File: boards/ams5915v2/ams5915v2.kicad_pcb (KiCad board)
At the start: 2 copper layers, 20 x 56.5 mm, 32 parts, among them J1 Conn_01x04, M3 MountingHole_3.2mm_M3, U1 TLV73333PDBVR, U2 MAX4995A, U3 AMS5915, U4 MAX4995A, U5 AMS5915

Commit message: [ams5915v2] new board design
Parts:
- removed 3v3: 3v3, Measurement_Points:Measurement_Point_Round-SMD-Pad_Small
- removed 5v: 5v, Measurement_Points:Measurement_Point_Round-SMD-Pad_Small
- removed GND: GND, Measurement_Points:Measurement_Point_Round-SMD-Pad_Small
- removed M3 (x3): MountingHole_3.2mm_M3, Mounting_Holes:MountingHole_3.2mm_M3
- added REF**: MountingHole_3.2mm_M3, Mounting_Holes:MountingHole_3.2mm_M3, F.Cu at (60.5, 77.5)
- added REF**: MountingHole_3.2mm_M3, Mounting_Holes:MountingHole_3.2mm_M3, F.Cu at (83.0, 68.0)
- added REF**: MountingHole_3.2mm_M3, Mounting_Holes:MountingHole_3.2mm_M3, F.Cu at (105.5, 77.5)
- added TP1: 5v, Measurement_Points:Measurement_Point_Round-SMD-Pad_Small, F.Cu at (105.4, 65.0)
- added TP2: GND, Measurement_Points:Measurement_Point_Round-SMD-Pad_Small, F.Cu at (103.7, 72.9)
- added TP3: 3v3, Measurement_Points:Measurement_Point_Round-SMD-Pad_Small, B.Cu at (96.5, 66.5)
- C1, C2, C3, C4, C5, C6, C7, C8, R1, R2, R5, R6, R7, R8, U1, U2, U4: moved to B.Cu
- moved R7 119.7 mm to (65.9, 75.9), turned to 90 degrees
- moved C8 118.0 mm to (69.2, 76.7)
- moved D4 117.3 mm to (62.2, 70.0), turned to 270 degrees
- moved U5 115.6 mm to (64.2, 80.0), turned to 0 degrees
- moved U4 115.0 mm to (68.8, 73.7), turned to 90 degrees
- moved C5 111.8 mm to (71.5, 72.5), turned to 270 degrees
- moved C6 108.3 mm to (69.2, 78.4), turned to 180 degrees
- moved R8 107.0 mm to (73.0, 71.7)
- moved R5 103.9 mm to (88.4, 75.8), turned to 90 degrees
- moved C7 103.0 mm to (91.6, 76.7)
- moved D3 101.7 mm to (84.3, 73.8), turned to 180 degrees
- moved U2 101.2 mm to (91.1, 73.8), turned to 90 degrees
- moved C3 99.2 mm to (92.8, 71.0)
- moved J1 98.6 mm to (107.1, 65.0), turned to 0 degrees
- moved R6 97.9 mm to (92.1, 69.7), turned to 0 degrees
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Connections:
- net /5v renamed +5V
- net /GND renamed GND
- U1 pad 4: Net-(U1-Pad4) -> (no net)
- U3 pad 5: Net-(U3-Pad5) -> (no net)
- U3 pad 6: Net-(U3-Pad6) -> (no net)
- U3 pad 7: Net-(U3-Pad7) -> (no net)
- U3 pad 8: Net-(U3-Pad8) -> (no net)
- U5 pad 5: Net-(U5-Pad5) -> (no net)
- U5 pad 6: Net-(U5-Pad6) -> (no net)
- U5 pad 7: Net-(U5-Pad7) -> (no net)
- U5 pad 8: Net-(U5-Pad8) -> (no net)
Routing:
- net +5V: track 94.2 -> 14.1 mm, vias 4 -> 0
- net GND: track 126.4 -> 197.9 mm, vias 39 -> 22
- net Net-(C6-Pad1): track 23.1 -> 5.72 mm
- net Net-(C4-Pad1): track 22.7 -> 5.68 mm
- net /3v3: track 64.9 -> 53.5 mm
- net Net-(D1-Pad1): track 12.0 -> 1.55 mm
- net Net-(D4-Pad1): track 1.40 -> 11.5 mm, vias 0 -> 1
- net Net-(D2-Pad2): track 10.5 -> 1.72 mm
- net Net-(D3-Pad1): track 1.25 -> 7.98 mm, vias 0 -> 1
- net Net-(R1-Pad2): track 39.0 -> 34.7 mm, vias 2 -> 1
- net Net-(R2-Pad2): track 39.3 -> 36.8 mm, vias 2 -> 0
- net Net-(R7-Pad2): track 3.54 -> 2.09 mm
- net Net-(R5-Pad2): track 3.28 -> 1.86 mm
- net Net-(R8-Pad2): track 3.87 -> 3.33 mm
- net Net-(R6-Pad2): track 3.82 -> 3.28 mm
- removed copper zone on B.Cu, net +5V
- removed copper zone on B.Cu, net /3v3
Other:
- board size 20 x 56.5 mm -> 52 x 17 mm
- net class Default: trace_width 0.6 -> 0.25
- board text added: "+3V3"
- board text added: "+5V"
- board text added: "GND"
- board text added: "Over current"
- board text added: "SCL SDA GND"
- board text added: "ams5915v2 RX-VIPER"
- board text removed: "5v"

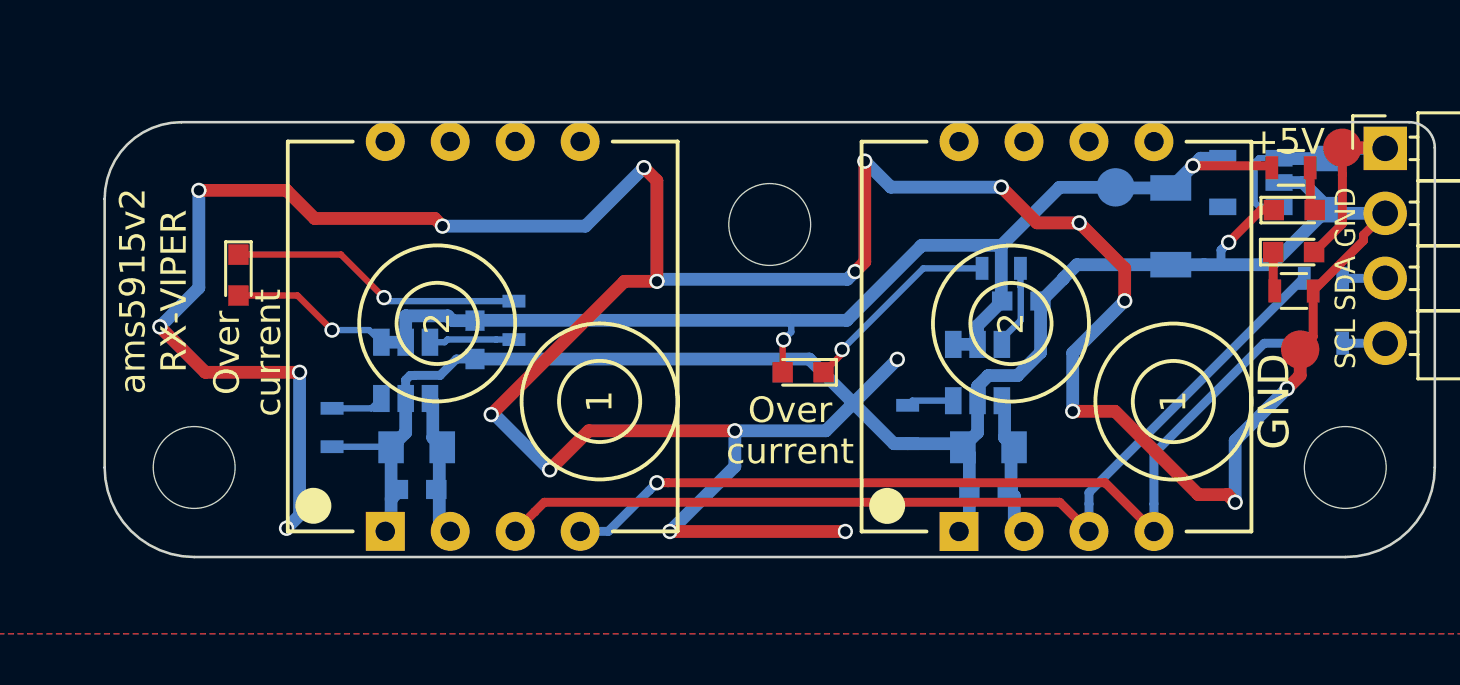
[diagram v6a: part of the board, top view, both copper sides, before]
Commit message: [ams5915v2] new board design: minor fixes
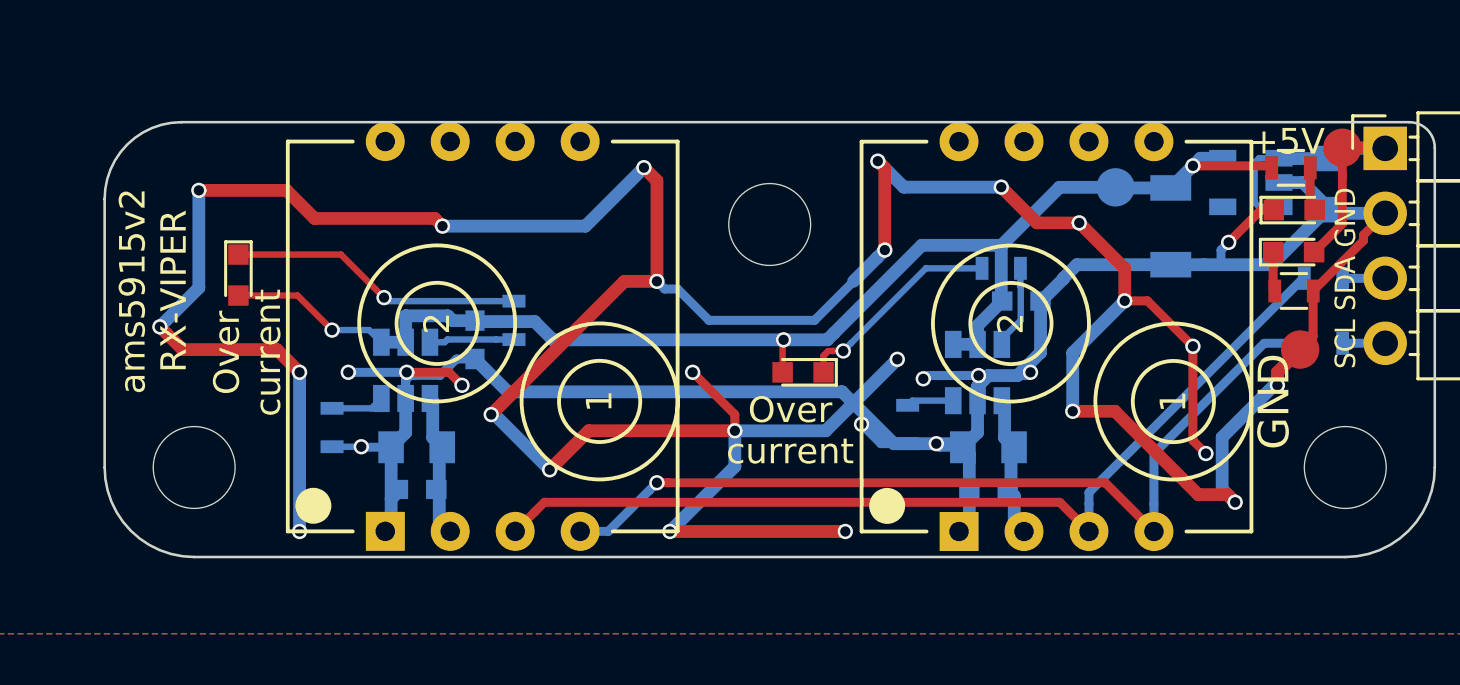
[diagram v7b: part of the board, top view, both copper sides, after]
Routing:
- net GND: track 197.9 -> 225.9 mm, vias 22 -> 34

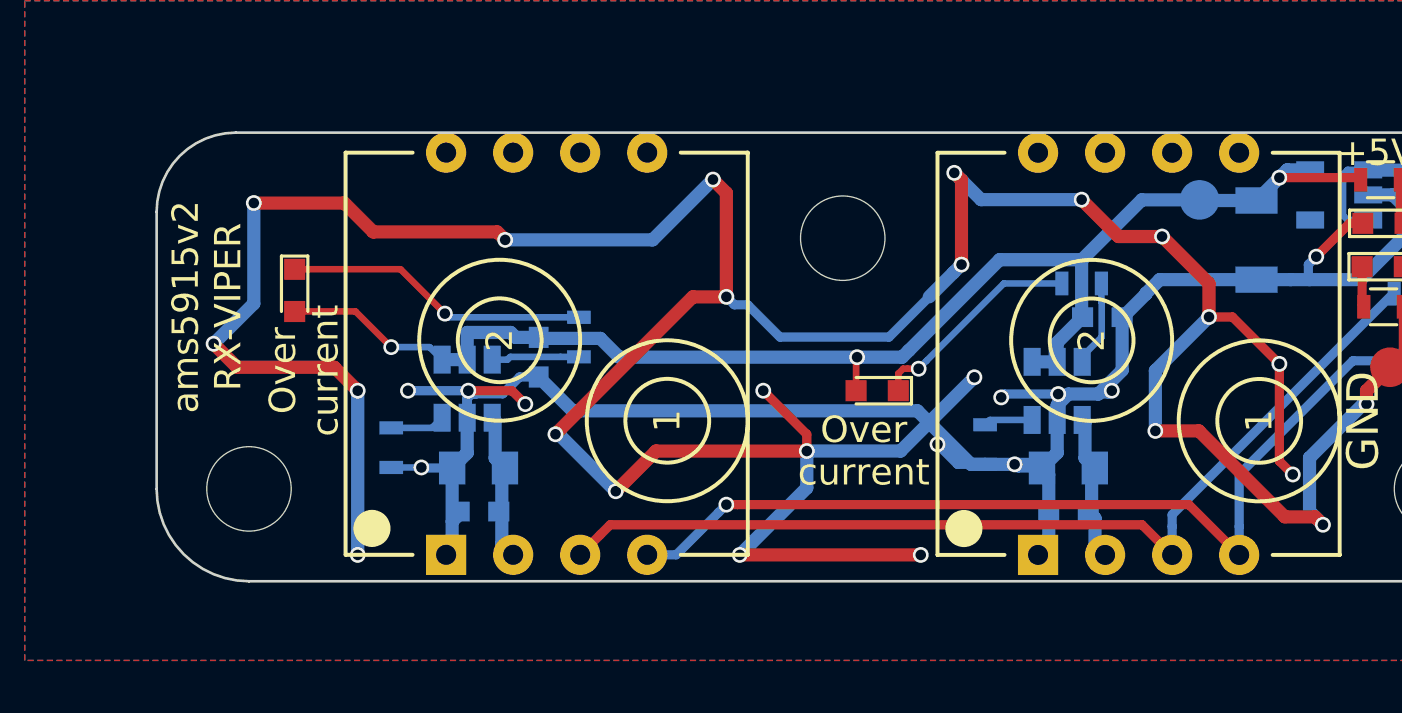
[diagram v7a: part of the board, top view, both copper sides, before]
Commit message: [ams5915v2] new board design: overcurrent leds in center of board
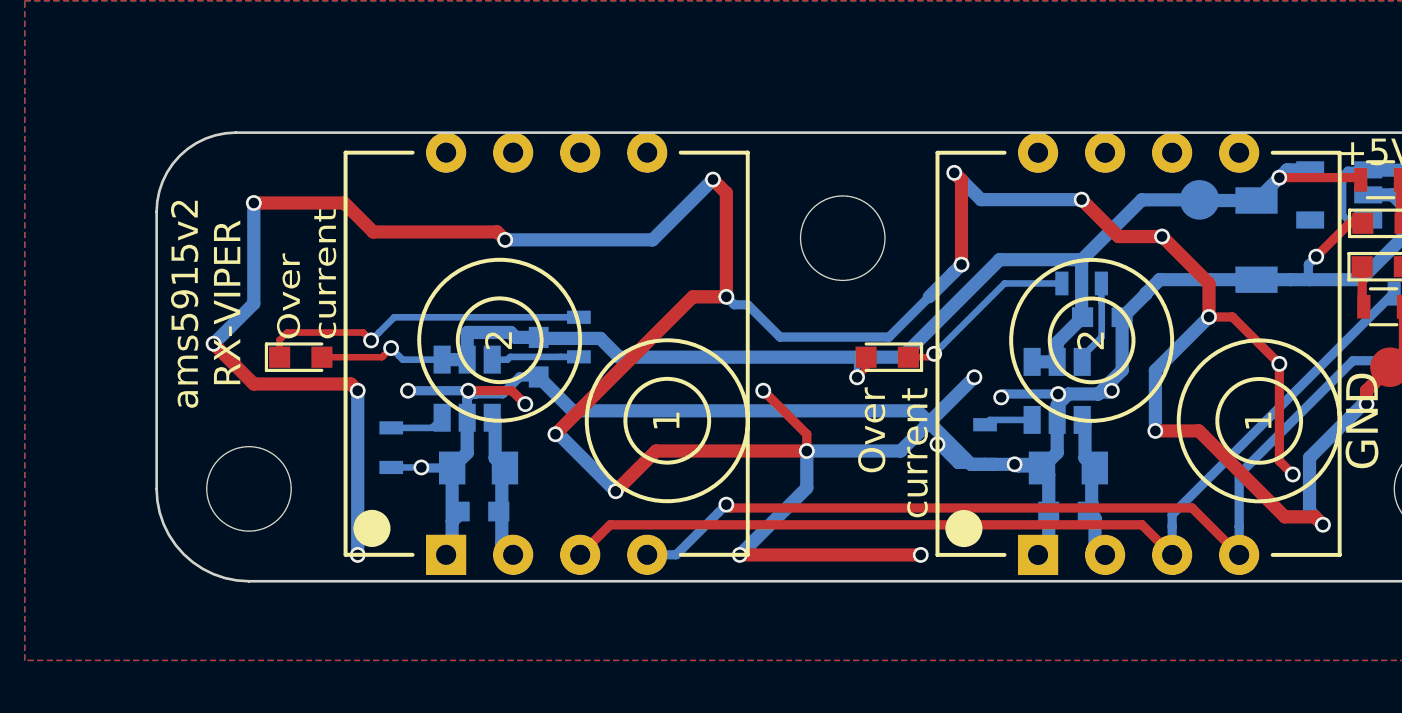
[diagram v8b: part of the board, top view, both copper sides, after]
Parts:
- moved D4 2.54 mm to (62.5, 72.5), turned to 0 degrees
- moved D3 1.33 mm to (84.7, 72.5)
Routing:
- net Net-(D3-Pad1): track 8.26 -> 6.97 mm
- net /3v3: track 53.3 -> 52.2 mm
- net Net-(D4-Pad1): track 11.5 -> 12.6 mm
